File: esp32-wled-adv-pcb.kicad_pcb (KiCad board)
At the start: 2 copper layers, 91.5 x 44.5 mm, 50 parts, among them J1 Conn_01x03_Male, J2 Conn_01x03_Male, J4 Screw_Terminal_01x02, J5 Conn_01x02, Q1 BS170F, SW1 SW_Push, SW2 SW_Push, U1 MT3420C, U2 ESP32-PICO-D4

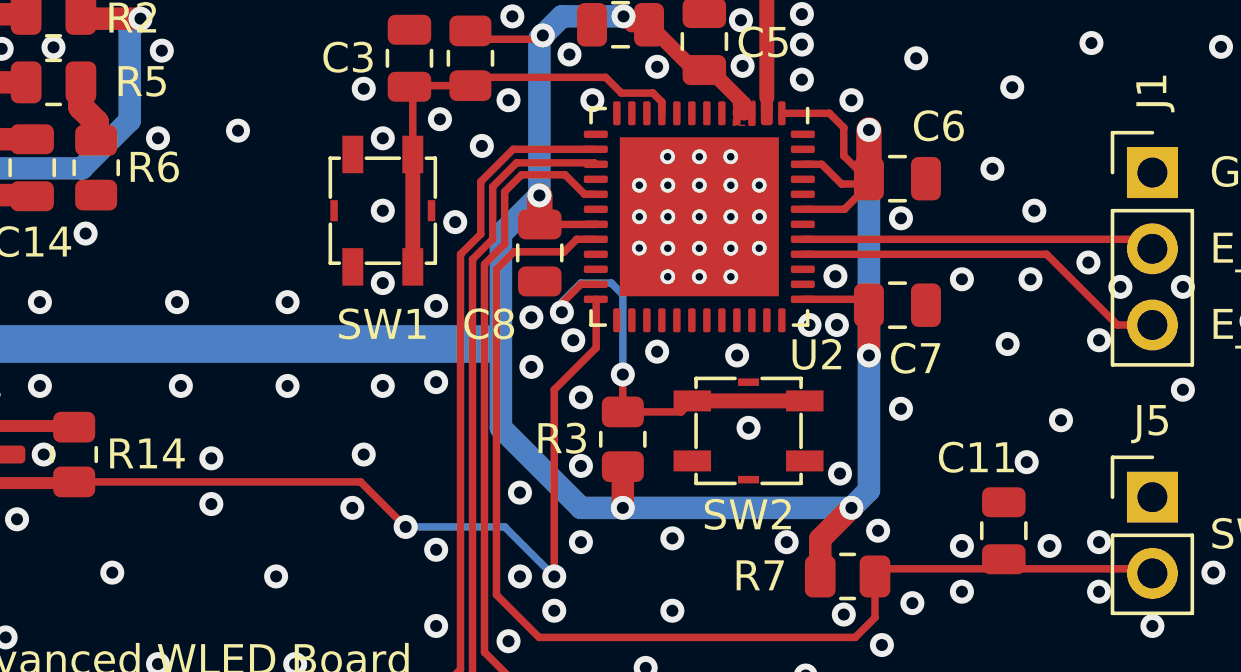
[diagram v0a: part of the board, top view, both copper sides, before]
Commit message: add missing silkscreen text for boot and reset switch, refresh schematic and images
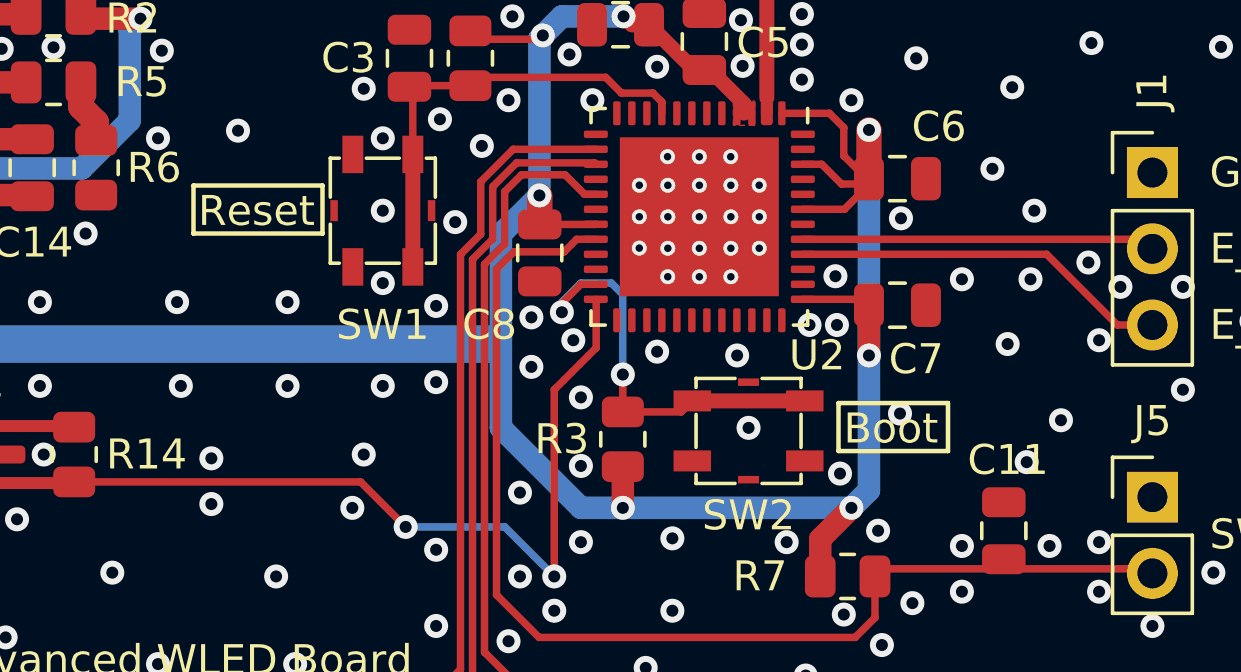
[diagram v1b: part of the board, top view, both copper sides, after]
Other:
- board text added: "Boot"
- board text added: "Reset"
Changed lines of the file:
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@@
       (drillshape 0)
       (scaleselection 1)
-      (outputdirectory "pdf/")
+      (outputdirectory "gerber/")
     )
   )
@@
     (fp_line (start 18.45 -2.05) (end 10.05 -2.05) (layer "F.Fab") (width 0.1))
     (fp_line (start -5.95 -13.2) (end 3.45 -13.2) (layer "F.Fab") (width 0.1))
-    (fp_line (start 3.55 -8.45) (end 9.95 -8.45) (layer "F.Fab") (width 0.1))
-    (fp_line (start 10.05 -2.05) (end 10.05 -7.95) (layer "F.Fab") (width 0.1))
     (fp_line (start -5.95 3.2) (end -5.95 -13.2) (layer "F.Fab") (width 0.1))
     (fp_line (start 9.95 -1.55) (end 3.55 -1.55) (layer "F.Fab") (width 0.1))
     (fp_line (start 18.45 -7.95) (end 18.45 -2.05) (layer "F.Fab") (width 0.1))
+    (fp_line (start 3.55 -8.45) (end 9.95 -8.45) (layer "F.Fab") (width 0.1))
     (fp_line (start 10.05 -7.95) (end 18.45 -7.95) (layer "F.Fab") (width 0.1))
+    (fp_line (start 10.05 -2.05) (end 10.05 -7.95) (layer "F.Fab") (width 0.1))
     (pad "1" thru_hole circle (at 0 0 270) (size 2.3 2.3) (drill 1.32) (layers *.Cu *.Mask)
       (net 54 "Net-(R10-Pad2)") (pinfunction "1") (pintype "passive"))
@@
     (fp_line (start 18.5 -8) (end 18.5 -2) (layer "F.SilkS") (width 0.1))
     (fp_line (start 10 -1.5) (end 10 -8.5) (layer "F.SilkS") (width 0.1))
-    (fp_line (start 10 -2) (end 18.5 -2) (layer "F.SilkS") (width 0.1))
     (fp_line (start 3.5 -13.25) (end -6 -13.25) (layer "F.SilkS") (width 0.1))
-    (fp_line (start 3.5 3.25) (end 3.5 -13.25) (layer "F.SilkS") (width 0.1))
     (fp_line (start 10 -8.5) (end 3.5 -8.5) (layer "F.SilkS") (width 0.1))
-    (fp_line (start -6 3.25) (end 3.5 3.25) (layer "F.SilkS") (width 0.1))
     (fp_line (start 18.5 -8) (end 10 -8) (layer "F.SilkS") (width 0.1))
     (fp_line (start -6 -13.25) (end -6 3.25) (layer "F.SilkS") (width 0.1))
+    (fp_line (start 3.5 3.25) (end 3.5 -13.25) (layer "F.SilkS") (width 0.1))
     (fp_line (start 3.5 -1.5) (end 10 -1.5) (layer "F.SilkS") (width 0.1))
+    (fp_line (start -6 3.25) (end 3.5 3.25) (layer "F.SilkS") (width 0.1))
+    (fp_line (start 10 -2) (end 18.5 -2) (layer "F.SilkS") (width 0.1))
     (fp_line (start 18.7 -13.4) (end -6.1 -13.4) (layer "F.CrtYd") (width 0.05))
     (fp_line (start -6.1 -13.4) (end -6.1 3.4) (layer "F.CrtYd") (width 0.05))
@@
     (property "Sheetname" "")
     (attr smd)
-    (fp_text reference "C11" (at 2.413 -0.889 180) (layer "F.SilkS")
+    (fp_text reference "C11" (at 2.356 0.139 180) (layer "F.SilkS")
       (effects (font (size 1 1) (thickness 0.15)))
     )
@@
   )
   (gr_line (start 90.043 107.569) (end 81.915 107.569) (layer "F.SilkS") (width 0.15))
+  (gr_rect (start 130.85 100) (end 135.15 101.6) (layer "F.SilkS") (width 0.15) (fill none))
+  (gr_rect (start 152.35 107.25) (end 156 108.85) (layer "F.SilkS") (width 0.15) (fill none))
   (gr_rect (start 81.25 86.5) (end 172.75 131) (layer "Edge.Cuts") (width 0.1) (fill none))
   (gr_text "LED" (at 83.312 100.076 90) (layer "F.SilkS")
@@
     (effects (font (size 2 2) (thickness 0.25)))
   )
+  (gr_text "Boot" (at 154.1 108.1) (layer "F.SilkS")
+    (effects (font (size 1 1) (thickness 0.15)))
+  )
+  (gr_text "Reset" (at 132.95 100.85) (layer "F.SilkS")
+    (effects (font (size 1 1) (thickness 0.15)))
+  )
   (gr_text "+5V" (at 90.043 115.062) (layer "F.SilkS")
     (effects (font (size 1.5 1.5) (thickness 0.3)) (justify right))
@@
   (via (at 146.658755 103.04036) (size 0.5) (drill 0.25) (layers "F.Cu" "B.Cu") (net 2))
   (via (at 171.704 116.84) (size 0.8) (drill 0.4) (layers "F.Cu" "B.Cu") (free) (net 2))
-  (via (at 154.432 107.442) (size 0.8) (drill 0.4) (layers "F.Cu" "B.Cu") (free) (net 2))
+  (via (at 154.4 107.6) (size 0.8) (drill 0.4) (layers "F.Cu" "B.Cu") (free) (net 2))
   (via (at 82.296 130.048) (size 0.8) (drill 0.4) (layers "F.Cu" "B.Cu") (free) (net 2))
   (via (at 143.383 95.631) (size 0.8) (drill 0.4) (layers "F.Cu" "B.Cu") (free) (net 2))
